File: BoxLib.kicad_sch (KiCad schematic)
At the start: 10 parts, among them J1 Generic_2Pos_terminal_block, J2 Solder-Jumper-NO, J3 Solder-Jumper-NO, J4 Solder-Jumper-NO, J5 Solder-Jumper-NC, J6 Solder-Jumper-NC, J7 Solder-Jumper-NC, J8 Solder-Jumper-NO, J9 Solder-Jumper-NC

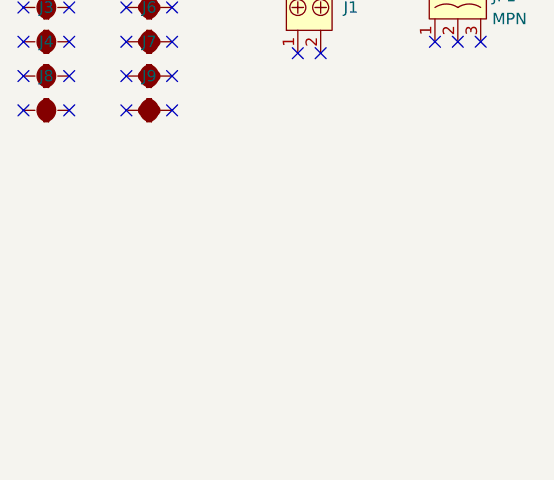
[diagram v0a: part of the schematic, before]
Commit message: Updated some fuses
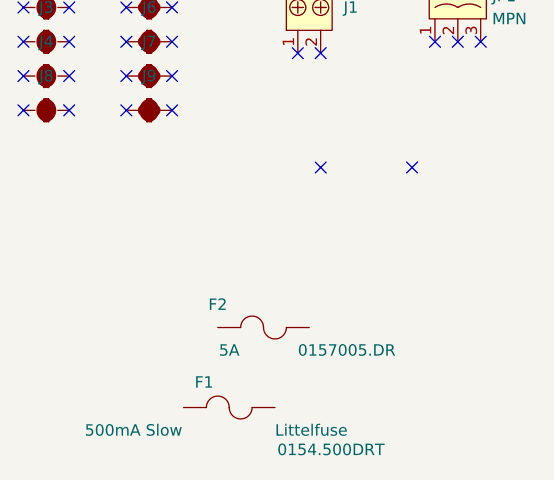
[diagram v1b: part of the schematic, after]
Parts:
- added F1: Littelfuse_154_0.5A_Slow, BoxLib:Fuse-Current-Littelfuse-Nano2_154, symbol BoxLib-Fuses:Littelfuse_154_0.5A_Slow
- added F2: 0157005.DR, BoxLib:Nano2-157, symbol BoxLib-Fuses:0157005.DR
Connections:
- no-connect marks 21 -> 23
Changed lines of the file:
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@@
   (no_connect (at 92.71 69.85))
   (no_connect (at 87.63 69.85))
+  (no_connect (at 120.65 76.2))
+  (no_connect (at 130.81 76.2))
   (no_connect (at 120.65 63.5))
   (no_connect (at 133.35 62.23))
@@
     (pin "2")
   )
+  (symbol (lib_id "BoxLib-Fuses:0157005.DR") (at 114.3 93.98 0) (unit 1)
+    (in_bom yes) (on_board yes)
+    (property "Reference" "F2" (id 0) (at 109.22 91.44 0))
+    (property "Value" "0157005.DR" (id 1) (at 118.11 96.52 0)
+      (effects (font (size 1.27 1.27)) (justify left))
+    )
+    (property "Footprint" "BoxLib:Nano2-157" (id 2) (at 114.3 97.79 0)
+      (effects (font (size 1.27 1.27)) hide)
+    )
+    (property "Datasheet" "https://www.littelfuse.com/~/media/electronics/datasheets/fuses/littelfuse_fuse_157t_datasheet.pdf.pdf" (id 3) (at 114.3 93.98 0)
+      (effects (font (size 1.27 1.27)) hide)
+    )
+    (property "Current" "5A" (id 4) (at 110.49 96.52 0))
+    (pin "1")
+    (pin "2")
+  )
   (symbol (lib_name "Solder-Jumper-NO_2") (lib_id "BoxLib-Headers:Solder-Jumper-NO") (at 90.17 62.23 0) (unit 1)
     (in_bom no) (on_board yes) (fields_autoplaced)
@@
     (pin "2")
   )
+  (symbol (lib_id "BoxLib-Fuses:Littelfuse_154_0.5A_Slow") (at 110.49 102.87 0) (unit 1)
+    (in_bom yes) (on_board yes)
+    (property "Reference" "F1" (id 0) (at 107.696 100.076 0))
+    (property "Value" "Littelfuse_154_0.5A_Slow" (id 1) (at 110.49 102.87 0)
+      (effects (font (size 1.27 1.27)) hide)
+    )
+    (property "Footprint" "BoxLib:Fuse-Current-Littelfuse-Nano2_154" (id 2) (at 110.49 102.87 0)
+      (effects (font (size 1.27 1.27)) hide)
+    )
+    (property "Datasheet" "https://m.littelfuse.com/~/media/electronics/datasheets/fuses/littelfuse_fuse_154_154t_154l_154tl_datasheet.pdf.pdf" (id 3) (at 110.49 102.997 0)
+      (effects (font (size 1.27 1.27)) hide)
+    )
+    (property "Current" "500mA Slow" (id 4) (at 105.283 105.41 0)
+      (effects (font (size 1.27 1.27)) (justify right))
+    )
+    (property "Manufacturer" "Littelfuse" (id 5) (at 115.57 105.41 0)
+      (effects (font (size 1.27 1.27)) (justify left))
+    )
+    (property "MPN" "0154.500DRT" (id 6) (at 115.824 107.569 0)
+      (effects (font (size 1.27 1.27)) (justify left))
+    )
+    (property "Replace With" "454.5" (id 7) (at 110.49 102.997 0)
+      (effects (font (size 1.27 1.27)) hide)
+    )
+    (property "Octopart" "" (id 8) (at 110.49 102.87 0)
+      (effects (font (size 1.27 1.27)) hide)
+    )
+    (pin "1")
+    (pin "2")
+  )
   (sheet_instances
     (path "/" (page "1"))
   )
   (symbol_instances
+    (path "/f4e92608-53ba-49a5-880c-443776c87820"
+      (reference "F1") (unit 1) (value "Littelfuse_154_0.5A_Slow") (footprint "BoxLib:Fuse-Current-Littelfuse-Nano2_154")
+    )
+    (path "/32f708e0-df94-44e7-a6ae-cda54a0cd338"
+      (reference "F2") (unit 1) (value "0157005.DR") (footprint "BoxLib:Nano2-157")
+    )
     (path "/55fec84c-f38b-4c24-8678-bb8ae45083f8"
       (reference "J1") (unit 1) (value "Generic_2Pos_terminal_block") (footprint "BoxLib:PTH-2-1_5mmx2mmx5mm")

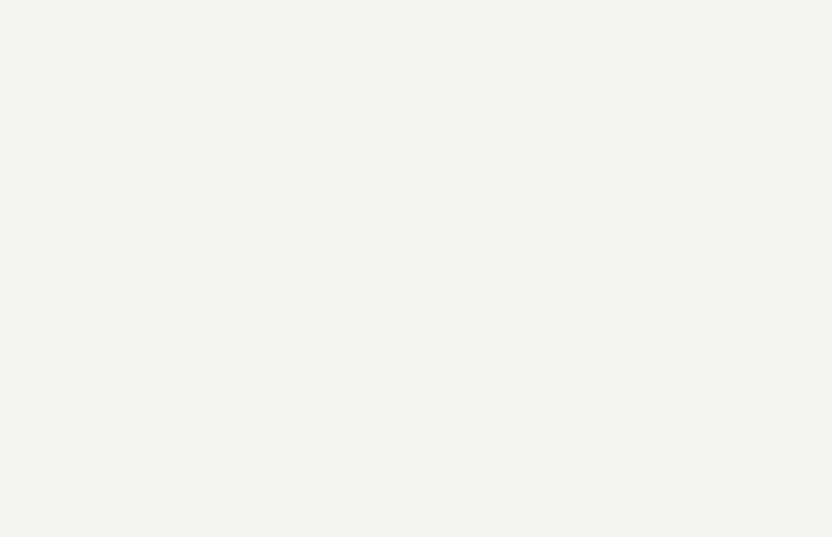
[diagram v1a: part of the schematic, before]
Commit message: Added a couple of Adafruit QT Pys
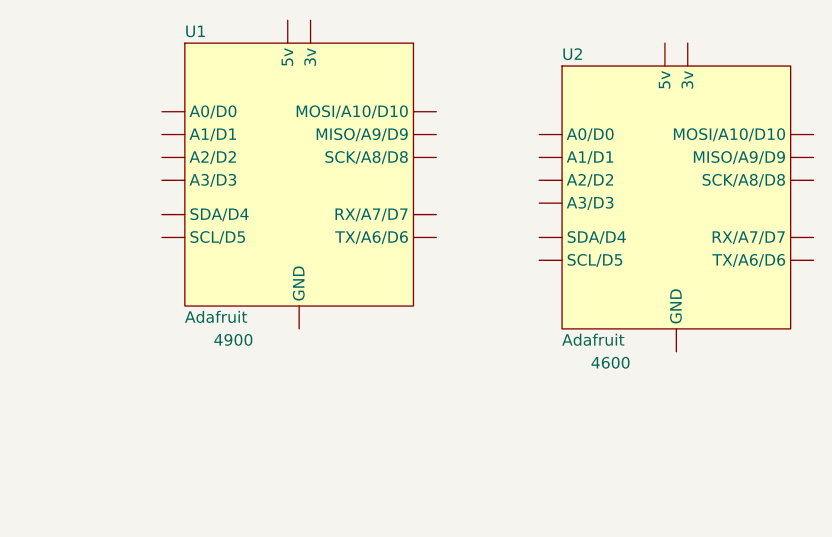
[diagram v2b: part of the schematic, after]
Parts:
- added U1: (no value), symbol BoxLib-Adafruit:QT_Py_RP2040
- added U2: (no value), symbol BoxLib-Adafruit:QT_Py
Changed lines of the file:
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@@
     (pin "3")
+  )
+  (symbol (lib_id "BoxLib-Adafruit:QT_Py") (at 245.11 69.85 0) (unit 1)
+    (in_bom yes) (on_board yes)
+    (property "Reference" "U2" (id 0) (at 232.41 53.34 0)
+      (effects (font (size 1.27 1.27)) (justify left))
+    )
+    (property "Value" "" (id 1) (at 257.81 85.09 0)
+      (effects (font (size 1.27 1.27)) (justify right))
+    )
+    (property "Footprint" "" (id 2) (at 245.11 38.1 0)
+      (effects (font (size 1.27 1.27)) hide)
+    )
+    (property "Datasheet" "https://www.adafruit.com/product/4600" (id 3) (at 245.11 40.64 0)
+      (effects (font (size 1.27 1.27)) hide)
+    )
+    (property "MPN" "4600" (id 4) (at 240.03 87.63 0)
+      (effects (font (size 1.27 1.27)) (justify right))
+    )
+    (property "Manufacturer" "Adafruit" (id 5) (at 232.41 85.09 0)
+      (effects (font (size 1.27 1.27)) (justify left))
+    )
+    (property "A0 Pin" "A0" (id 6) (at 245.11 69.85 0)
+      (effects (font (size 1.27 1.27)) hide)
+    )
+    (property "A1 Pin" "A1" (id 7) (at 245.11 69.85 0)
+      (effects (font (size 1.27 1.27)) hide)
+    )
+    (property "A2 Pin" "A2" (id 8) (at 245.11 69.85 0)
+      (effects (font (size 1.27 1.27)) hide)
+    )
+    (property "A3 Pin" "A3" (id 9) (at 245.11 69.85 0)
+      (effects (font (size 1.27 1.27)) hide)
+    )
+    (property "SDA Pin" "SDA" (id 10) (at 245.11 69.85 0)
+      (effects (font (size 1.27 1.27)) hide)
+    )
+    (property "SCL Pin" "SCL" (id 11) (at 245.11 69.85 0)
+      (effects (font (size 1.27 1.27)) hide)
+    )
+    (property "TX Pin" "TX" (id 12) (at 245.11 69.85 0)
+      (effects (font (size 1.27 1.27)) hide)
+    )
+    (property "RX Pin" "RX" (id 13) (at 245.11 69.85 0)
+      (effects (font (size 1.27 1.27)) hide)
+    )
+    (property "SCK Pin" "SCK" (id 14) (at 245.11 69.85 0)
+      (effects (font (size 1.27 1.27)) hide)
+    )
+    (property "MISO Pin" "MISO" (id 15) (at 245.11 69.85 0)
+      (effects (font (size 1.27 1.27)) hide)
+    )
+    (property "MOSI Pin" "MOSI" (id 16) (at 245.11 69.85 0)
+      (effects (font (size 1.27 1.27)) hide)
+    )
+    (property "3v Pin" "3v" (id 17) (at 245.11 69.85 0)
+      (effects (font (size 1.27 1.27)) hide)
+    )
+    (property "GND Pin" "GND" (id 18) (at 245.11 69.85 0)
+      (effects (font (size 1.27 1.27)) hide)
+    )
+    (property "5v Pin" "5v" (id 19) (at 245.11 69.85 0)
+      (effects (font (size 1.27 1.27)) hide)
+    )
+    (pin "3v")
+    (pin "5v")
+    (pin "A0")
+    (pin "A1")
+    (pin "A2")
+    (pin "A3")
+    (pin "GND")
+    (pin "MISO")
+    (pin "MOSI")
+    (pin "RX")
+    (pin "SCK")
+    (pin "SCL")
+    (pin "SDA")
+    (pin "TX")
   )
   (symbol (lib_id "BoxLib-Headers:Solder-Jumper-NO") (at 90.17 58.42 0) (unit 1)
@@
     (pin "2")
   )
+  (symbol (lib_id "BoxLib-Adafruit:QT_Py_RP2040") (at 203.2 67.31 0) (unit 1)
+    (in_bom yes) (on_board yes)
+    (property "Reference" "U1" (id 0) (at 190.5 50.8 0)
+      (effects (font (size 1.27 1.27)) (justify left))
+    )
+    (property "Value" "" (id 1) (at 215.9 82.55 0)
+      (effects (font (size 1.27 1.27)) (justify right))
+    )
+    (property "Footprint" "" (id 2) (at 203.2 35.56 0)
+      (effects (font (size 1.27 1.27)) hide)
+    )
+    (property "Datasheet" "https://www.adafruit.com/product/4900" (id 3) (at 203.2 38.1 0)
+      (effects (font (size 1.27 1.27)) hide)
+    )
+    (property "MPN" "4900" (id 4) (at 198.12 85.09 0)
+      (effects (font (size 1.27 1.27)) (justify right))
+    )
+    (property "Manufacturer" "Adafruit" (id 5) (at 190.5 82.55 0)
+      (effects (font (size 1.27 1.27)) (justify left))
+    )
+    (property "A0 Pin" "A0" (id 6) (at 203.2 67.31 0)
+      (effects (font (size 1.27 1.27)) hide)
+    )
+    (property "A1 Pin" "A1" (id 7) (at 203.2 67.31 0)
+      (effects (font (size 1.27 1.27)) hide)
+    )
+    (property "A2 Pin" "A2" (id 8) (at 203.2 67.31 0)
+      (effects (font (size 1.27 1.27)) hide)
+    )
+    (property "A3 Pin" "A3" (id 9) (at 203.2 67.31 0)
+      (effects (font (size 1.27 1.27)) hide)
+    )
+    (property "SDA Pin" "SDA" (id 10) (at 203.2 67.31 0)
+      (effects (font (size 1.27 1.27)) hide)
+    )
+    (property "SCL Pin" "SCL" (id 11) (at 203.2 67.31 0)
+      (effects (font (size 1.27 1.27)) hide)
+    )
+    (property "TX Pin" "TX" (id 12) (at 203.2 67.31 0)
+      (effects (font (size 1.27 1.27)) hide)
+    )
+    (property "RX Pin" "RX" (id 13) (at 203.2 67.31 0)
+      (effects (font (size 1.27 1.27)) hide)
+    )
+    (property "SCK Pin" "SCK" (id 14) (at 203.2 67.31 0)
+      (effects (font (size 1.27 1.27)) hide)
+    )
+    (property "MISO Pin" "MISO" (id 15) (at 203.2 67.31 0)
+      (effects (font (size 1.27 1.27)) hide)
+    )
+    (property "MOSI Pin" "MOSI" (id 16) (at 203.2 67.31 0)
+      (effects (font (size 1.27 1.27)) hide)
+    )
+    (property "3v Pin" "3v" (id 17) (at 203.2 67.31 0)
+      (effects (font (size 1.27 1.27)) hide)
+    )
+    (property "GND Pin" "GND" (id 18) (at 203.2 67.31 0)
+      (effects (font (size 1.27 1.27)) hide)
+    )
+    (property "5v Pin" "5v" (id 19) (at 203.2 67.31 0)
+      (effects (font (size 1.27 1.27)) hide)
+    )
+    (pin "3v")
+    (pin "5v")
+    (pin "A0")
+    (pin "A1")
+    (pin "A2")
+    (pin "A3")
+    (pin "GND")
+    (pin "MISO")
+    (pin "MOSI")
+    (pin "RX")
+    (pin "SCK")
+    (pin "SCL")
+    (pin "SDA")
+    (pin "TX")
+  )
   (sheet_instances
     (path "/" (page "1"))
@@
       (reference "JP1") (unit 1) (value "Jumper-3-Pos") (footprint "BoxLib:Header-3pos-0.5in-1.27mm-Harwin-M50-3530342")
     )
-  )
+    (path "/feb25c34-5b2e-4610-8c3a-964823b2348a"
+      (reference "U1") (unit 1) (value "QT_Py_RP2040") (footprint "BoxLib:Adafruit-QT_Py_RP2040-PTH")
+    )
+    (path "/6de99912-7afe-4fd9-8cfb-4bf27c16ae93"
+      (reference "U2") (unit 1) (value "QT_Py") (footprint "")
+    )
+  )

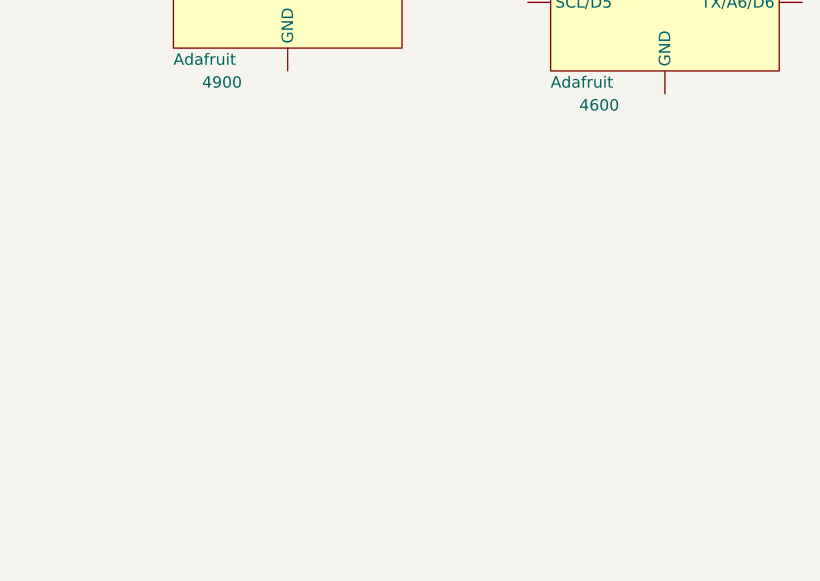
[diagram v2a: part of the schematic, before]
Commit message: Added Adafruit 4383 Display
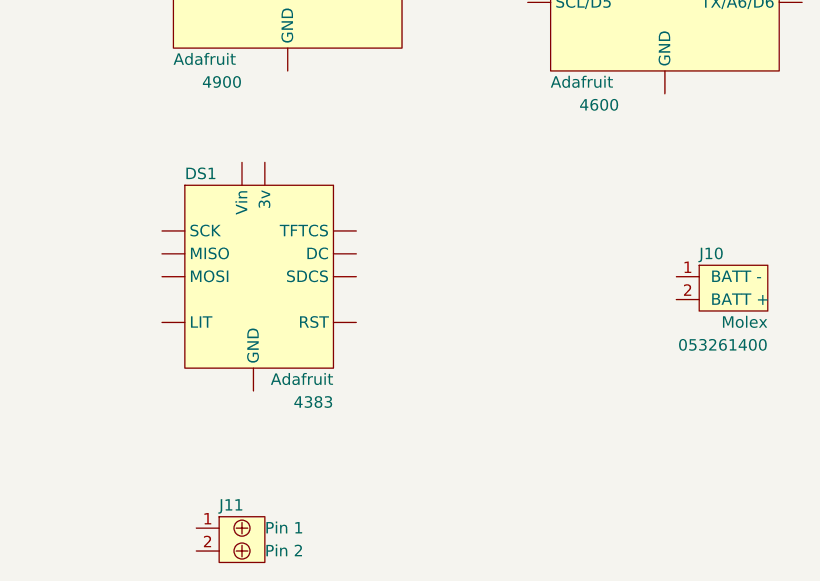
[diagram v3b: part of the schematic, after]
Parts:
- added DS1: (no value), symbol BoxLib-Displays:Adafruit-4383
- added J10: (no value), symbol BoxLib-Connectors:Molex_2Pos_terminal_block_1.25mm-0532614002
- added J11: (no value), symbol BoxLib-Connectors:Generic_2Pos_terminal_block
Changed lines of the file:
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@@
+    (pin "2")
+  )
+  (symbol (lib_id "BoxLib-Connectors:Molex_2Pos_terminal_block_1.25mm-0532614002") (at 251.46 106.68 0) (unit 1)
+    (in_bom yes) (on_board yes)
+    (property "Reference" "J10" (id 0) (at 248.92 104.14 0)
+      (effects (font (size 1.27 1.27)) (justify left))
+    )
+    (property "Value" "" (id 1) (at 254 100.33 0)
+      (effects (font (size 1.27 1.27)) hide)
+    )
+    (property "Footprint" "" (id 2) (at 246.38 101.6 0)
+      (effects (font (size 1.27 1.27)) hide)
+    )
+    (property "Datasheet" "" (id 3) (at 248.92 109.855 0)
+      (effects (font (size 1.27 1.27)) hide)
+    )
+    (property "Pin1" "BATT -" (id 4) (at 250.19 106.68 0)
+      (effects (font (size 1.27 1.27)) (justify left))
+    )
+    (property "Pin2" "BATT +" (id 5) (at 250.19 109.22 0)
+      (effects (font (size 1.27 1.27)) (justify left))
+    )
+    (property "Manufacturer" "Molex" (id 6) (at 256.54 111.76 0)
+      (effects (font (size 1.27 1.27)) (justify right))
+    )
+    (property "MPN" "053261400" (id 7) (at 256.54 114.3 0)
+      (effects (font (size 1.27 1.27)) (justify right))
+    )
+    (pin "1")
     (pin "2")
   )
@@
     (pin "2")
   )
+  (symbol (lib_id "BoxLib-Displays:Adafruit-4383") (at 199.39 105.41 0) (unit 1)
+    (in_bom yes) (on_board yes)
+    (property "Reference" "DS1" (id 0) (at 191.77 95.25 0)
+      (effects (font (size 1.27 1.27)) (justify left))
+    )
+    (property "Value" "" (id 1) (at 199.39 77.47 0)
+      (effects (font (size 1.27 1.27)) hide)
+    )
+    (property "Footprint" "" (id 2) (at 200.66 80.01 0)
+      (effects (font (size 1.27 1.27)) hide)
+    )
+    (property "Datasheet" "" (id 3) (at 185.42 87.63 0)
+      (effects (font (size 1.27 1.27)) hide)
+    )
+    (property "Manufacturer" "Adafruit" (id 4) (at 208.28 118.11 0)
+      (effects (font (size 1.27 1.27)) (justify right))
+    )
+    (property "MPN" "4383" (id 5) (at 208.28 120.65 0)
+      (effects (font (size 1.27 1.27)) (justify right))
+    )
+    (pin "3v")
+    (pin "DC")
+    (pin "GND")
+    (pin "LIT")
+    (pin "MISO")
+    (pin "MOSI")
+    (pin "RST")
+    (pin "SCK")
+    (pin "SDCS")
+    (pin "TFTCS")
+    (pin "Vin")
+  )
+  (symbol (lib_id "BoxLib-Connectors:Generic_2Pos_terminal_block") (at 198.12 134.62 0) (unit 1)
+    (in_bom yes) (on_board yes)
+    (property "Reference" "J11" (id 0) (at 195.58 132.08 0)
+      (effects (font (size 1.27 1.27)) (justify left))
+    )
+    (property "Value" "" (id 1) (at 198.12 139.7 0)
+      (effects (font (size 1.27 1.27)) hide)
+    )
+    (property "Footprint" "" (id 2) (at 195.58 137.795 0)
+      (effects (font (size 1.27 1.27)) hide)
+    )
+    (property "Datasheet" "" (id 3) (at 195.58 137.795 0)
+      (effects (font (size 1.27 1.27)) hide)
+    )
+    (property "Pin1" "Pin 1" (id 4) (at 200.66 134.62 0)
+      (effects (font (size 1.27 1.27)) (justify left))
+    )
+    (property "Pin2" "Pin 2" (id 5) (at 200.66 137.16 0)
+      (effects (font (size 1.27 1.27)) (justify left))
+    )
+    (pin "1")
+    (pin "2")
+  )
   (symbol (lib_name "Solder-Jumper-NC_3") (lib_id "BoxLib-Headers:Solder-Jumper-NC") (at 101.6 58.42 0) (unit 1)
     (in_bom no) (on_board yes) (fields_autoplaced)
@@
   )
   (symbol_instances
+    (path "/98ca5169-231d-4f6e-bb1a-cdb364a5a08d"
+      (reference "DS1") (unit 1) (value "Adafruit-4383") (footprint "BoxLib:Adafruit-1_14-tft-display-4383")
+    )
     (path "/f4e92608-53ba-49a5-880c-443776c87820"
       (reference "F1") (unit 1) (value "Littelfuse_154_0.5A_Slow") (footprint "BoxLib:Fuse-Current-Littelfuse-Nano2_154")
@@
       (reference "J9") (unit 1) (value "Solder-Jumper-NC") (footprint "BoxLib:Jumper-Solder-2mm-NC")
     )
+    (path "/129efeea-89d0-48ff-b5f5-9339477a2b2c"
+      (reference "J10") (unit 1) (value "Molex_2Pos_terminal_block_1.25mm-0532614002") (footprint "BoxLib:Connector-SMD-2Pos-Molex-0532614002")
+    )
+    (path "/b96dd37f-05c4-499e-81a9-5c68a476b74c"
+      (reference "J11") (unit 1) (value "Generic_2Pos_terminal_block") (footprint "BoxLib:Connector-SMD-2Pos-Wago-2060-452_998-404")
+    )
     (path "/6558fe1b-a3c8-432c-ad80-f285a01e900f"
       (reference "JP1") (unit 1) (value "Jumper-3-Pos") (footprint "BoxLib:Header-3pos-0.5in-1.27mm-Harwin-M50-3530342")
@@
     )
     (path "/6de99912-7afe-4fd9-8cfb-4bf27c16ae93"
-      (reference "U2") (unit 1) (value "QT_Py") (footprint "")
-    )
-  )
+      (reference "U2") (unit 1) (value "QT_Py") (footprint "BoxLib:Adafruit-QT_Py-PTH")
+    )
+  )
